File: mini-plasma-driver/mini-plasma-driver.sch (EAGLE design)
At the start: 93 parts, among them IC1 IR21844D, IC2 74LS19N, IC3 NE555N, IC5 IR21844D, J1 12v IN, Q1 IRF640, Q2 IRF640, Q3 2N2369, Q4 2N2369, Q5 IRF640, Q6 IRF640

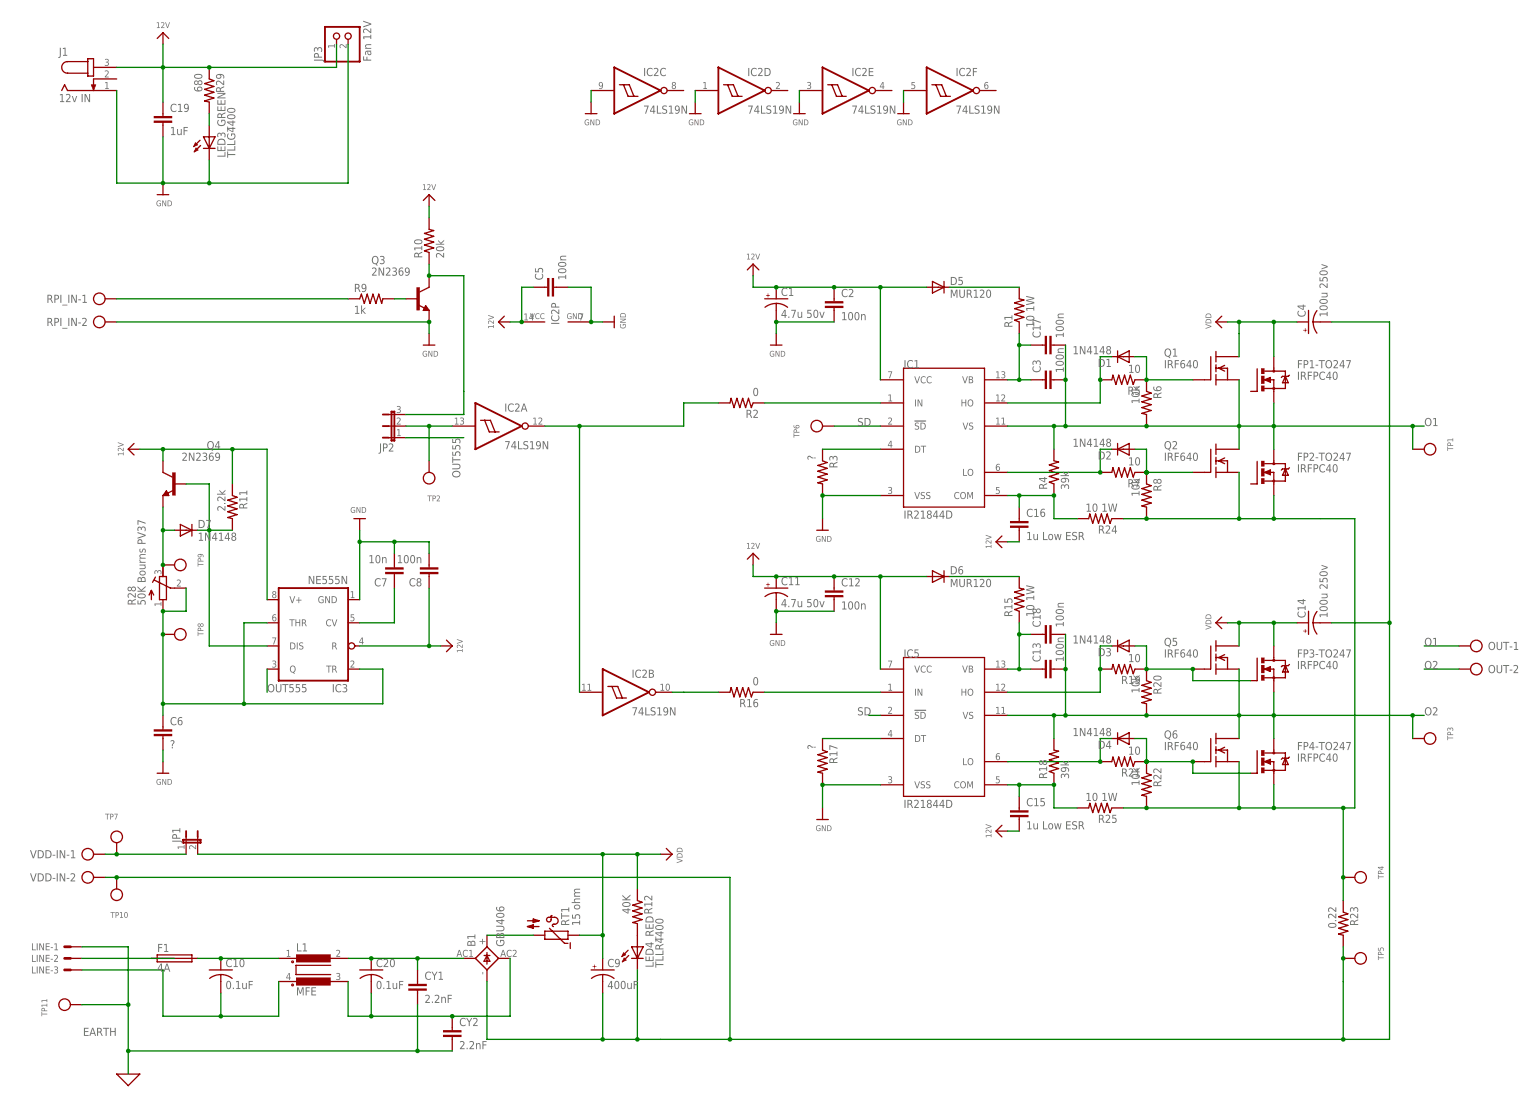
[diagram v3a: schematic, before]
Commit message: First pass at placement, with schematic tweaks. Size of board not specified; Choke L1 drawing pinouts are incorrect + need to verif footprint
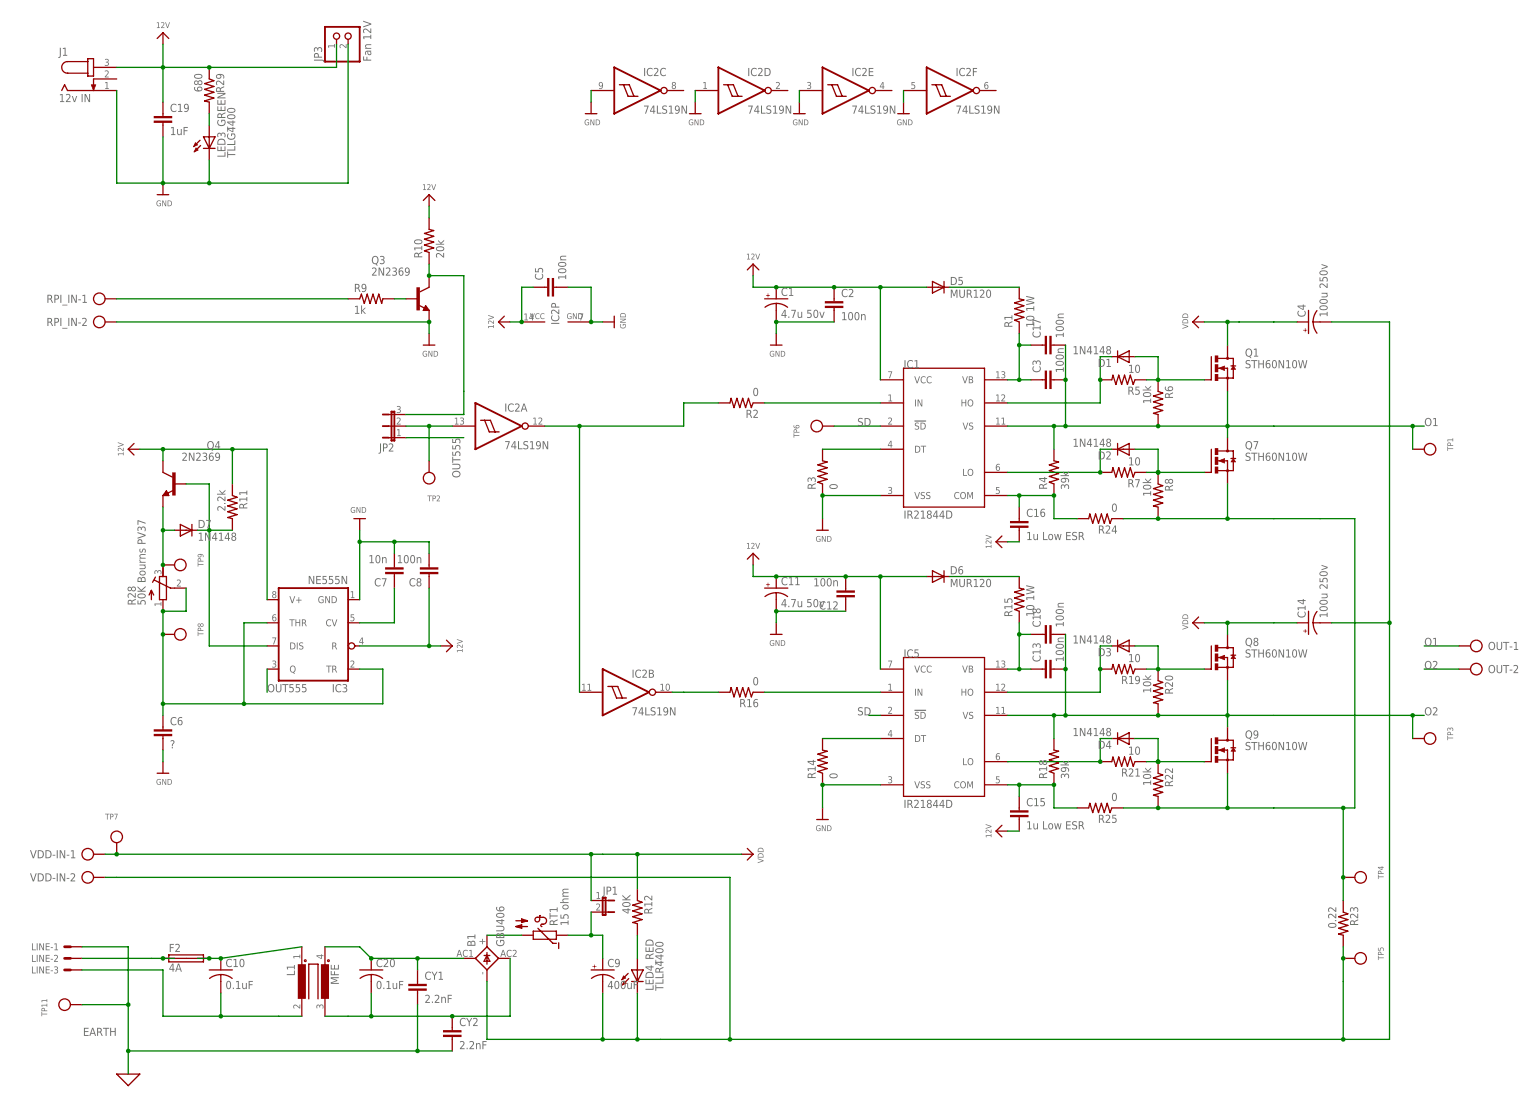
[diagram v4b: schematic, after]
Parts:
- removed F1: 4A, fuse:SH22,5A
- removed FP1-TO247, FP2-TO247, FP3-TO247, FP4-TO247: IRFPC40, transistor-power:IRFPC40
- removed Q2, Q5, Q6: IRF640, transistor-fet:IRF620
- removed R17: ?, rcl:R-US_0207/10
- removed TP10: (no value), microbuilder:TESTPOINT0.1"
- added F2: 4A, fuse:SHK20Q
- added Q7, Q8, Q9: STH60N10W, transistor-power:STH60N10W
- added R14: 0, rcl:R-US_0309/V
- Q1: value IRF640 -> STH60N10W; device transistor-fet:IRF620 -> transistor-power:STH60N10W
- R24, R25: value 10 1W -> 0
- R3: value ? -> 0; device rcl:R-US_0207/10 -> rcl:R-US_0309/V
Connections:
- removed net N$33: JP1.1, TP7.P$1, VDD-IN-1.KL
- new net N$2: C9.+, JP1.2, RT1.1
- net 12V: now also C12.2; no longer C12.1
- net GND: now also C12.1, R14.1, R3.1; no longer C12.2, R17.2, R3.2
- net N$18: now also F2.2A, F2.2B; no longer F1.2
- net N$19: now also F2.1A, F2.1B; no longer F1.1
- net N$20: now also L1.3; no longer L1.2
- net N$22: now also L1.2; no longer L1.3
- net N$26: now also R14.2; no longer R17.1
- net N$28: now also Q8.G; no longer FP3-TO247.G, Q5.G
- net N$30: now also Q9.G; no longer FP4-TO247.G, Q6.G
- net N$35: now also Q7.S, Q9.S; no longer FP2-TO247.S, FP4-TO247.S, Q2.S, Q6.S
- net N$6: now also R3.2; no longer R3.1
- net N$9: now also Q7.G; no longer Q2.G
- net O1: now also Q7.D; no longer FP1-TO247.S, FP2-TO247.D, Q2.D
- net O2: now also Q8.S, Q9.D; no longer FP3-TO247.S, FP4-TO247.D, Q5.S, Q6.D
- net VDD: now also JP1.1, Q8.D, TP7.P$1, VDD-IN-1.KL; no longer C9.+, FP1-TO247.D, FP3-TO247.D, JP1.2, Q5.D, RT1.1
- net VDD-: no longer TP10.P$1
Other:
- moved on the sheet: C12, JP1, L1, LED4_RED, R20, R22, R3, R6, R8, RT1

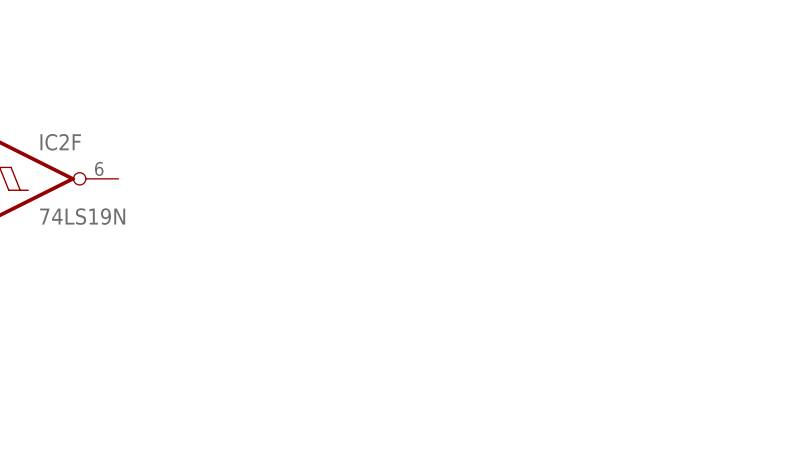
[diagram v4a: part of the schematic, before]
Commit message: add mounting holes
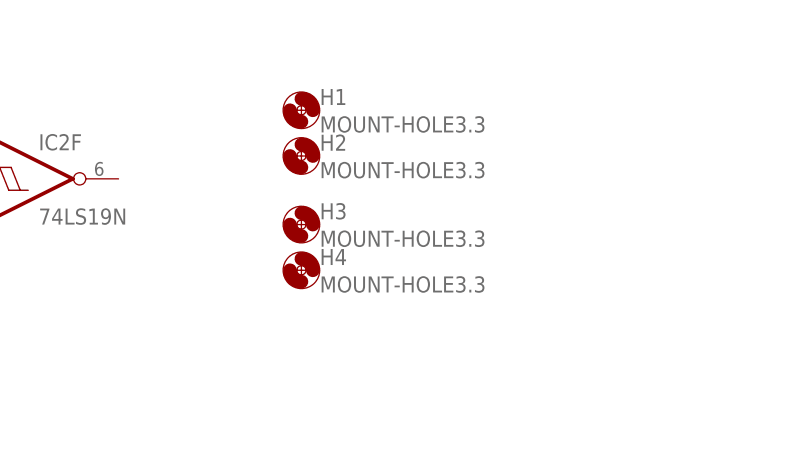
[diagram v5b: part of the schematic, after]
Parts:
- added H1, H2, H3, H4: MOUNT-HOLE3.3, holes:MOUNT-HOLE3.3
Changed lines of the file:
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@@
 <grid distance="0.1" unitdist="inch" unit="inch" style="lines" multiple="1" display="no" altdistance="0.01" altunitdist="inch" altunit="inch"/>
 <layers>
-<layer number="1" name="Top" color="4" fill="1" visible="yes" active="no"/>
-<layer number="2" name="Route2" color="1" fill="3" visible="yes" active="no"/>
-<layer number="3" name="Route3" color="4" fill="3" visible="yes" active="no"/>
-<layer number="4" name="Route4" color="1" fill="4" visible="yes" active="no"/>
-<layer number="5" name="Route5" color="4" fill="4" visible="yes" active="no"/>
-<layer number="6" name="Route6" color="1" fill="8" visible="yes" active="no"/>
-<layer number="7" name="Route7" color="4" fill="8" visible="yes" active="no"/>
-<layer number="8" name="Route8" color="1" fill="2" visible="yes" active="no"/>
-<layer number="9" name="Route9" color="4" fill="2" visible="yes" active="no"/>
-<layer number="10" name="Route10" color="1" fill="7" visible="yes" active="no"/>
-<layer number="11" name="Route11" color="4" fill="7" visible="yes" active="no"/>
-<layer number="12" name="Route12" color="1" fill="5" visible="yes" active="no"/>
-<layer number="13" name="Route13" color="4" fill="5" visible="yes" active="no"/>
-<layer number="14" name="Route14" color="1" fill="6" visible="yes" active="no"/>
-<layer number="15" name="Route15" color="4" fill="6" visible="yes" active="no"/>
-<layer number="16" name="Bottom" color="1" fill="1" visible="yes" active="no"/>
-<layer number="17" name="Pads" color="2" fill="1" visible="yes" active="no"/>
-<layer number="18" name="Vias" color="2" fill="1" visible="yes" active="no"/>
-<layer number="19" name="Unrouted" color="6" fill="1" visible="yes" active="no"/>
-<layer number="20" name="Dimension" color="24" fill="1" visible="yes" active="no"/>
-<layer number="21" name="tPlace" color="7" fill="1" visible="yes" active="no"/>
-<layer number="22" name="bPlace" color="7" fill="1" visible="yes" active="no"/>
-<layer number="23" name="tOrigins" color="15" fill="1" visible="yes" active="no"/>
-<layer number="24" name="bOrigins" color="15" fill="1" visible="yes" active="no"/>
-<layer number="25" name="tNames" color="7" fill="1" visible="yes" active="no"/>
-<layer number="26" name="bNames" color="7" fill="1" visible="yes" active="no"/>
-<layer number="27" name="tValues" color="7" fill="1" visible="yes" active="no"/>
-<layer number="28" name="bValues" color="7" fill="1" visible="yes" active="no"/>
+<layer number="1" name="Top" color="4" fill="1" visible="no" active="no"/>
+<layer number="2" name="Route2" color="1" fill="3" visible="no" active="no"/>
+<layer number="3" name="Route3" color="4" fill="3" visible="no" active="no"/>
+<layer number="4" name="Route4" color="1" fill="4" visible="no" active="no"/>
+<layer number="5" name="Route5" color="4" fill="4" visible="no" active="no"/>
+<layer number="6" name="Route6" color="1" fill="8" visible="no" active="no"/>
+<layer number="7" name="Route7" color="4" fill="8" visible="no" active="no"/>
+<layer number="8" name="Route8" color="1" fill="2" visible="no" active="no"/>
+<layer number="9" name="Route9" color="4" fill="2" visible="no" active="no"/>
+<layer number="10" name="Route10" color="1" fill="7" visible="no" active="no"/>
+<layer number="11" name="Route11" color="4" fill="7" visible="no" active="no"/>
+<layer number="12" name="Route12" color="1" fill="5" visible="no" active="no"/>
+<layer number="13" name="Route13" color="4" fill="5" visible="no" active="no"/>
+<layer number="14" name="Route14" color="1" fill="6" visible="no" active="no"/>
+<layer number="15" name="Route15" color="4" fill="6" visible="no" active="no"/>
+<layer number="16" name="Bottom" color="1" fill="1" visible="no" active="no"/>
+<layer number="17" name="Pads" color="2" fill="1" visible="no" active="no"/>
+<layer number="18" name="Vias" color="2" fill="1" visible="no" active="no"/>
+<layer number="19" name="Unrouted" color="6" fill="1" visible="no" active="no"/>
+<layer number="20" name="Dimension" color="24" fill="1" visible="no" active="no"/>
+<layer number="21" name="tPlace" color="7" fill="1" visible="no" active="no"/>
+<layer number="22" name="bPlace" color="7" fill="1" visible="no" active="no"/>
+<layer number="23" name="tOrigins" color="15" fill="1" visible="no" active="no"/>
+<layer number="24" name="bOrigins" color="15" fill="1" visible="no" active="no"/>
+<layer number="25" name="tNames" color="7" fill="1" visible="no" active="no"/>
+<layer number="26" name="bNames" color="7" fill="1" visible="no" active="no"/>
+<layer number="27" name="tValues" color="7" fill="1" visible="no" active="no"/>
+<layer number="28" name="bValues" color="7" fill="1" visible="no" active="no"/>
 <layer number="29" name="tStop" color="7" fill="3" visible="no" active="no"/>
 <layer number="30" name="bStop" color="7" fill="6" visible="no" active="no"/>
@@
 <layer number="35" name="tGlue" color="7" fill="4" visible="no" active="no"/>
 <layer number="36" name="bGlue" color="7" fill="5" visible="no" active="no"/>
-<layer number="37" name="tTest" color="7" fill="1" visible="yes" active="no"/>
-<layer number="38" name="bTest" color="7" fill="1" visible="yes" active="no"/>
+<layer number="37" name="tTest" color="7" fill="1" visible="no" active="no"/>
+<layer number="38" name="bTest" color="7" fill="1" visible="no" active="no"/>
 <layer number="39" name="tKeepout" color="4" fill="11" visible="no" active="no"/>
 <layer number="40" name="bKeepout" color="1" fill="11" visible="no" active="no"/>
@@
 <layer number="44" name="Drills" color="7" fill="1" visible="no" active="no"/>
 <layer number="45" name="Holes" color="7" fill="1" visible="no" active="no"/>
-<layer number="46" name="Milling" color="3" fill="1" visible="yes" active="no"/>
-<layer number="47" name="Measures" color="7" fill="1" visible="yes" active="no"/>
-<layer number="48" name="Document" color="7" fill="1" visible="yes" active="no"/>
-<layer number="49" name="Reference" color="7" fill="1" visible="yes" active="no"/>
-<layer number="50" name="dxf" color="7" fill="1" visible="yes" active="no"/>
-<layer number="51" name="tDocu" color="7" fill="1" visible="yes" active="no"/>
-<layer number="52" name="bDocu" color="7" fill="1" visible="yes" active="no"/>
-<layer number="53" name="tGND_GNDA" color="7" fill="9" visible="yes" active="no"/>
-<layer number="54" name="bGND_GNDA" color="1" fill="9" visible="yes" active="no"/>
-<layer number="56" name="wert" color="7" fill="1" visible="yes" active="no"/>
-<layer number="57" name="tCAD" color="7" fill="1" visible="yes" active="no"/>
-<layer number="58" name="bCAD" color="11" fill="1" visible="yes" active="no"/>
-<layer number="59" name="tCarbon" color="7" fill="1" visible="yes" active="no"/>
-<layer number="60" name="bCarbon" color="7" fill="1" visible="yes" active="no"/>
+<layer number="46" name="Milling" color="3" fill="1" visible="no" active="no"/>
+<layer number="47" name="Measures" color="7" fill="1" visible="no" active="no"/>
+<layer number="48" name="Document" color="7" fill="1" visible="no" active="no"/>
+<layer number="49" name="Reference" color="7" fill="1" visible="no" active="no"/>
+<layer number="50" name="dxf" color="7" fill="1" visible="no" active="no"/>
+<layer number="51" name="tDocu" color="7" fill="1" visible="no" active="no"/>
+<layer number="52" name="bDocu" color="7" fill="1" visible="no" active="no"/>
+<layer number="53" name="tGND_GNDA" color="7" fill="9" visible="no" active="no"/>
+<layer number="54" name="bGND_GNDA" color="1" fill="9" visible="no" active="no"/>
+<layer number="56" name="wert" color="7" fill="1" visible="no" active="no"/>
+<layer number="57" name="tCAD" color="7" fill="1" visible="no" active="no"/>
+<layer number="58" name="bCAD" color="11" fill="1" visible="no" active="no"/>
+<layer number="59" name="tCarbon" color="7" fill="1" visible="no" active="no"/>
+<layer number="60" name="bCarbon" color="7" fill="1" visible="no" active="no"/>
 <layer number="88" name="SimResults" color="9" fill="1" visible="yes" active="yes"/>
 <layer number="89" name="SimProbes" color="9" fill="1" visible="yes" active="yes"/>
@@
 <part name="R3" library="rcl" library_urn="urn:adsk.eagle:library:334" deviceset="R-US_" device="0309/V" package3d_urn="urn:adsk.eagle:package:23572/1" value="0"/>
 <part name="R14" library="rcl" library_urn="urn:adsk.eagle:library:334" deviceset="R-US_" device="0309/V" package3d_urn="urn:adsk.eagle:package:23572/1" value="0"/>
+<part name="H1" library="holes" library_urn="urn:adsk.eagle:library:237" deviceset="MOUNT-HOLE" device="3.3" package3d_urn="urn:adsk.eagle:package:14278/1"/>
+<part name="H2" library="holes" library_urn="urn:adsk.eagle:library:237" deviceset="MOUNT-HOLE" device="3.3" package3d_urn="urn:adsk.eagle:package:14278/1"/>
+<part name="H3" library="holes" library_urn="urn:adsk.eagle:library:237" deviceset="MOUNT-HOLE" device="3.3" package3d_urn="urn:adsk.eagle:package:14278/1"/>
+<part name="H4" library="holes" library_urn="urn:adsk.eagle:library:237" deviceset="MOUNT-HOLE" device="3.3" package3d_urn="urn:adsk.eagle:package:14278/1"/>
 </parts>
 <sheets>
@@
 <instance part="R3" gate="G$1" x="68.58" y="91.44" rot="R90"/>
 <instance part="R14" gate="G$1" x="68.58" y="27.94" rot="R90"/>
+<instance part="H1" gate="G$1" x="127" y="182.88"/>
+<instance part="H2" gate="G$1" x="127" y="177.8"/>
+<instance part="H3" gate="G$1" x="127" y="170.18"/>
+<instance part="H4" gate="G$1" x="127" y="165.1"/>
 </instances>
 <busses>

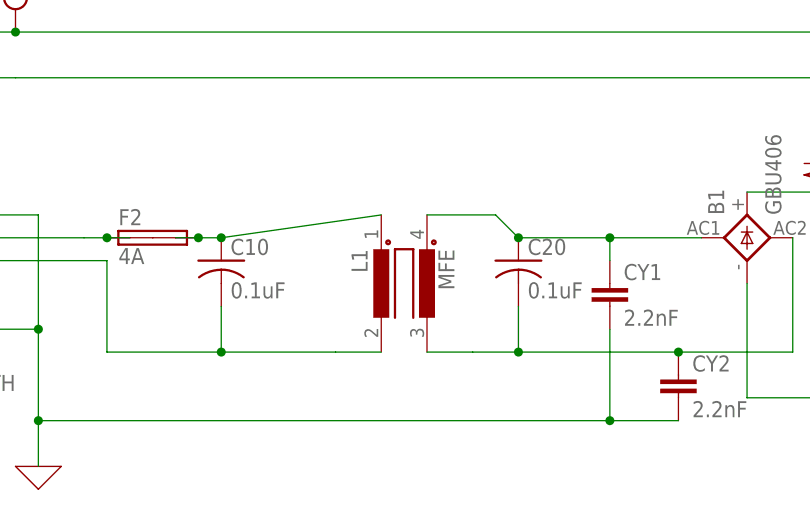
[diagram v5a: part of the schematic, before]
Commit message: ver. 7/27/18 20:15 corrected L1 package; placed TP11; gave driver DIPs more space for sockets.
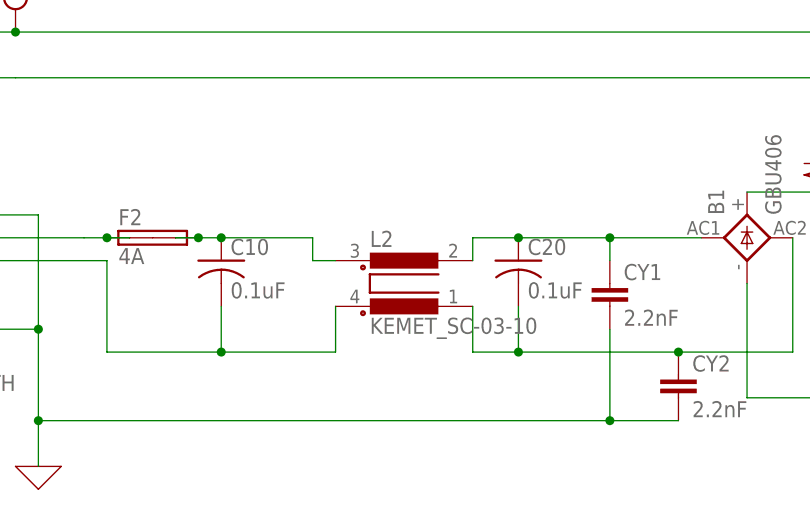
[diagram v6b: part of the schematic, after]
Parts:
- removed L1: MFE, inductors:MFE
- added L2: KEMET_SC-03-10, CdF Common:KEMET_SC-03-10
- TP11: device microbuilder:TESTPOINT0.1" -> microbuilder:TESTPOINTROUND2MM
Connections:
- net N$18: now also L2.1; no longer L1.1
- net N$20: now also L2.2; no longer L1.3
- net N$22: now also L2.3; no longer L1.2
- net N$31: now also L2.4; no longer L1.4
